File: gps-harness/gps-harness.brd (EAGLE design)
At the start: 29.6 x 33.9 mm, 7 parts

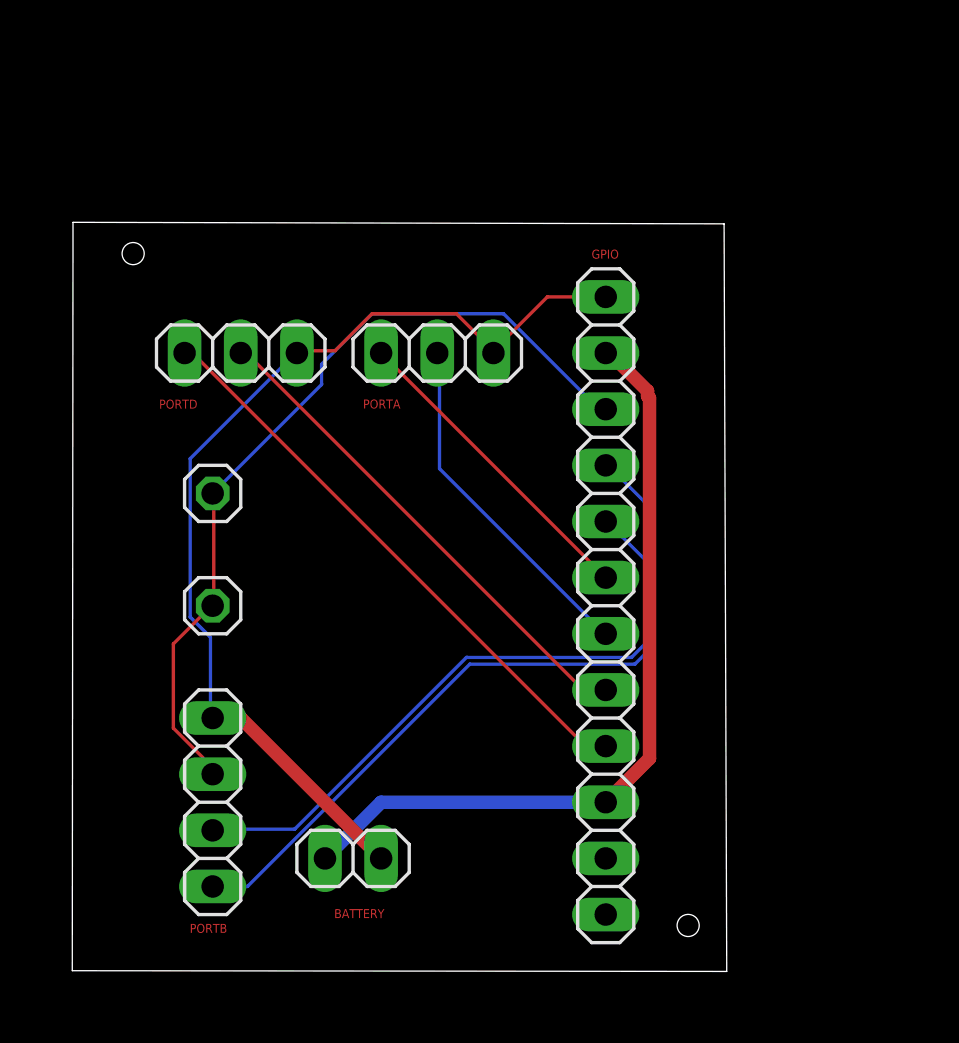
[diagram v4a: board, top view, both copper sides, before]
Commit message: Change Schematic to Parts by parts
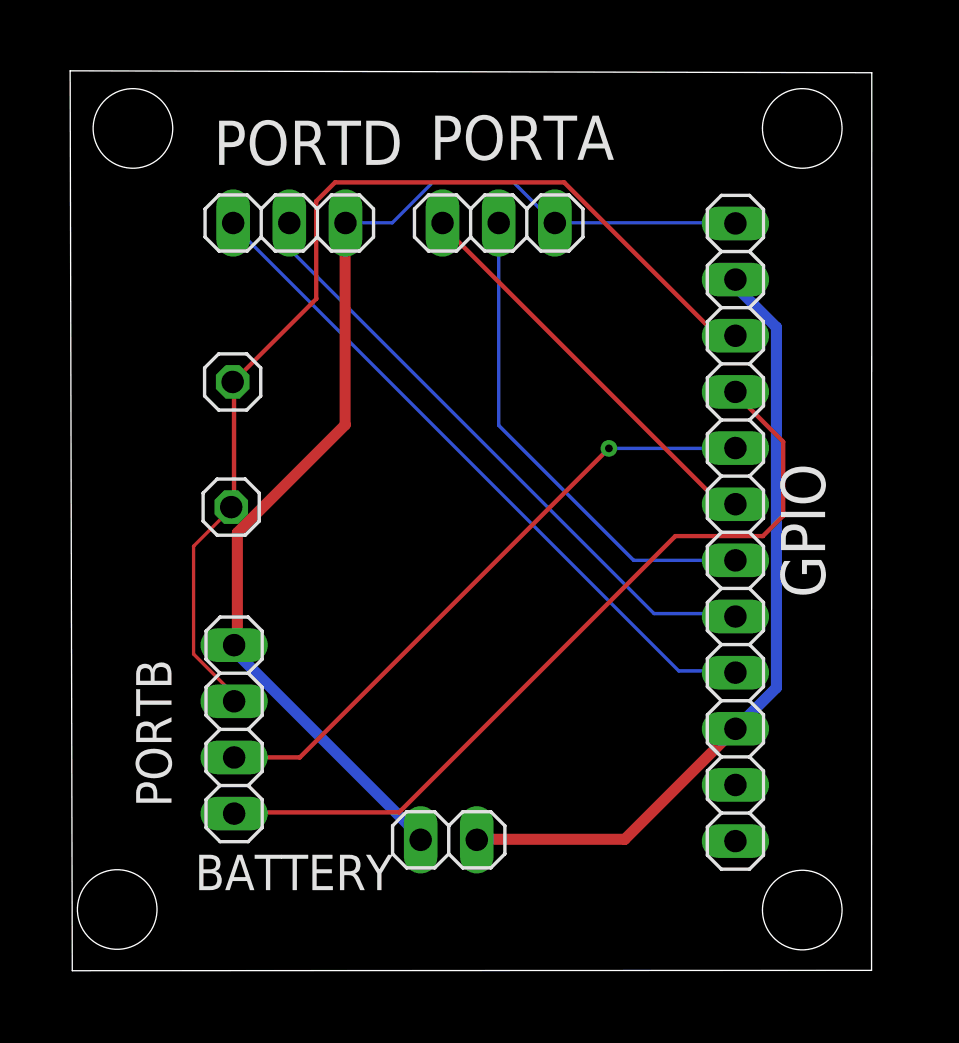
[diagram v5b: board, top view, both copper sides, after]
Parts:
- moved GPIO 6.74 mm to (30.0, 19.8)
- moved PORTA 6.51 mm to (19.3, 33.8)
- moved PORTD 6.28 mm to (9.82, 33.8)
- moved IMU 5.12 mm to (7.25, 26.6)
- moved TSY 4.54 mm to (7.19, 21.0)
- moved BATTERY 4.41 mm to (17.0, 5.92), turned to 180 degrees
- moved PORTB 3.44 mm to (7.32, 10.9)
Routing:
- net IMU: track 37.7 -> 47.9 mm
- net GND: track 45.8 -> 54.2 mm
- net RXA: track 15.9 -> 22.5 mm
- net RXD: track 22.9 -> 28.2 mm
- net TXD: track 26.4 -> 31.2 mm
- net TXA: track 14.4 -> 18.6 mm
- net TXB: track 33.5 -> 36.9 mm
- net RXB: track 29.3 -> 28.7 mm, vias 0 -> 1
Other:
- board size 29.6 x 33.9 mm -> 36.3 x 40.7 mm
- board text added: "Autorally GPS Harness v1.0 Oct. 2019"
- board text added: "IMU"
- board text added: "TSM"

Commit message: Reroute the board
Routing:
- net IMU: track 47.9 -> 39.9 mm, vias 0 -> 2
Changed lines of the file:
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@@
 <wire x1="7.3152" y1="12.192" x2="7.320278125" y2="12.186921875" width="0.1524" layer="1"/>
 <wire x1="7.1628" y1="20.8788" x2="7.1882" y2="20.9702375" width="0.1524" layer="1"/>
-<wire x1="29.1084" y1="28.8036" x2="29.8704" y2="28.8036" width="0.1524" layer="1"/>
-<wire x1="22.2504" y1="35.6616" x2="29.1084" y2="28.8036" width="0.2" layer="1"/>
-<wire x1="11.8872" y1="35.6616" x2="22.2504" y2="35.6616" width="0.2" layer="1"/>
-<wire x1="11.0363" y1="34.8107" x2="11.8872" y2="35.6616" width="0.2" layer="1"/>
-<wire x1="11.0363" y1="30.3911" x2="11.0363" y2="34.8107" width="0.2" layer="1"/>
-<wire x1="7.3152" y1="26.67" x2="11.0363" y2="30.3911" width="0.2" layer="1"/>
 <wire x1="29.8704" y1="28.8036" x2="29.9974" y2="28.722315625" width="0.1524" layer="1"/>
 <wire x1="7.3152" y1="26.67" x2="7.254240625" y2="26.6319" width="0.1524" layer="1"/>
+<wire x1="7.254240625" y1="26.6319" x2="13.30451875" y2="26.6319" width="0.1524" layer="16"/>
+<wire x1="13.30451875" y1="26.6319" x2="13.307059375" y2="26.634440625" width="0.1524" layer="16"/>
+<via x="13.307059375" y="26.634440625" extent="1-16" drill="0.35"/>
+<wire x1="13.307059375" y1="26.634440625" x2="17.983203125" y2="26.634440625" width="0.1524" layer="1"/>
+<wire x1="17.983203125" y1="26.634440625" x2="20.10918125" y2="28.76041875" width="0.1524" layer="1"/>
+<wire x1="20.10918125" y1="28.76041875" x2="20.114259375" y2="28.76041875" width="0.1524" layer="1"/>
+<via x="20.114259375" y="28.76041875" extent="1-16" drill="0.35"/>
+<wire x1="20.114259375" y1="28.76041875" x2="26.418540625" y2="28.76041875" width="0.1524" layer="16"/>
+<wire x1="26.418540625" y1="28.76041875" x2="26.42108125" y2="28.762959375" width="0.1524" layer="16"/>
+<wire x1="26.42108125" y1="28.762959375" x2="29.95675625" y2="28.762959375" width="0.1524" layer="16"/>
+<wire x1="29.95675625" y1="28.762959375" x2="29.9974" y2="28.722315625" width="0.1524" layer="16"/>
 </signal>
 <signal name="N$23">

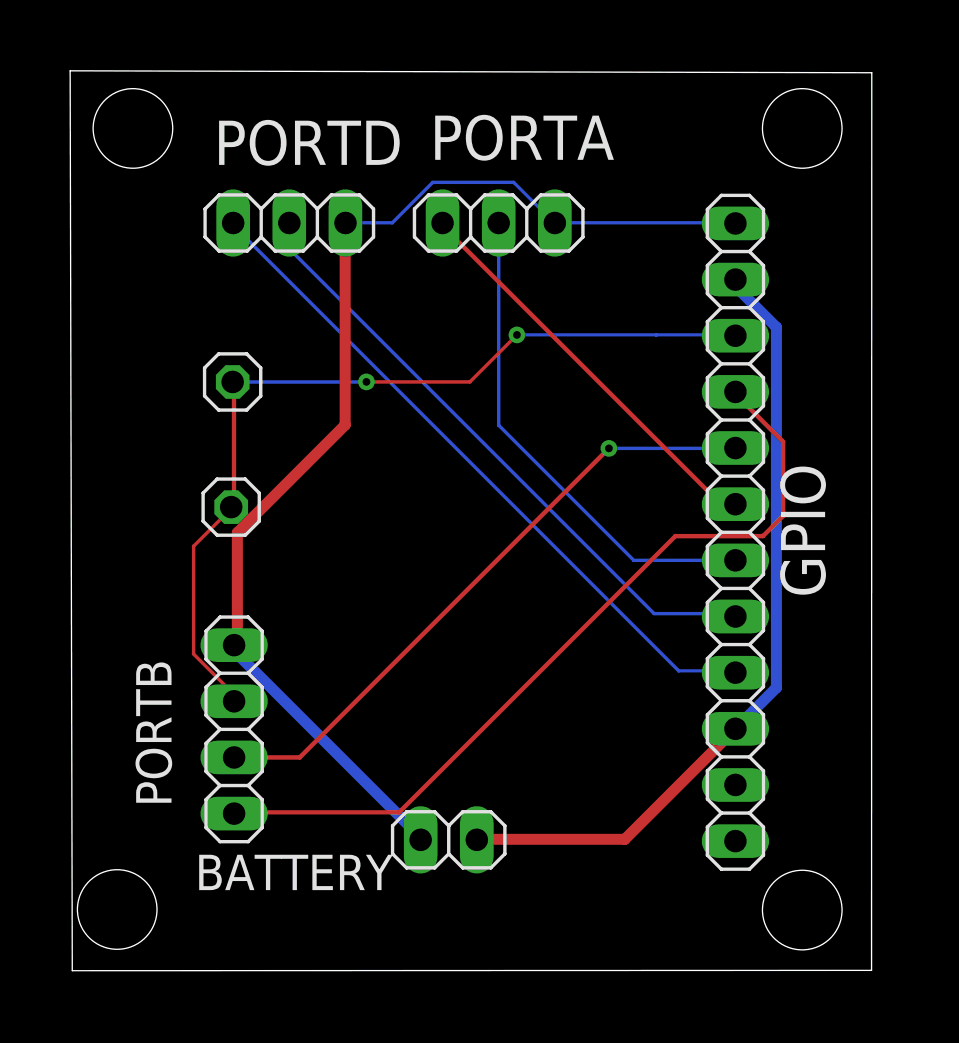
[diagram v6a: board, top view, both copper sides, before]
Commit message: Add GND Plane
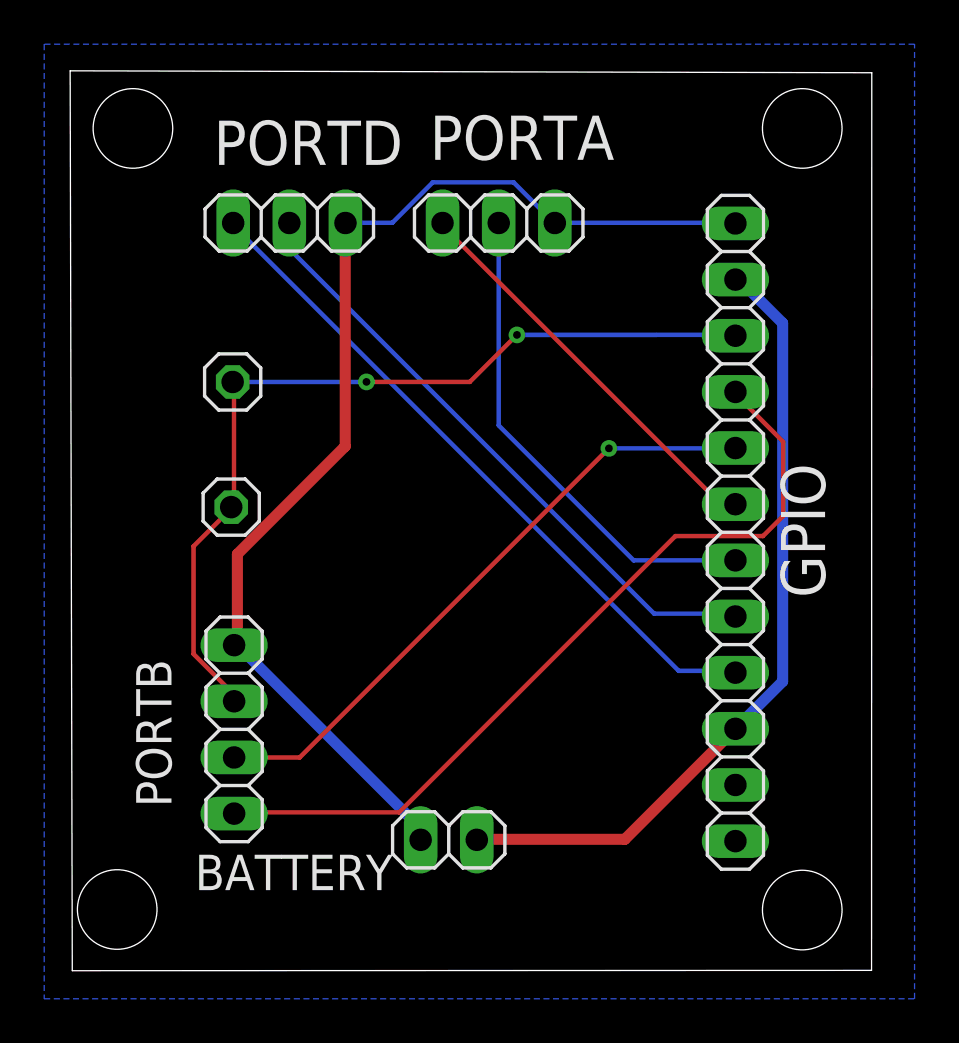
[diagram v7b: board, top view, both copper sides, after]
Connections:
- removed net N$23: GPIO.11
- removed net N$24: GPIO.12
- new net NO_CONNECTION: GPIO.11, GPIO.12
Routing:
- net GND: track 54.2 -> 53.3 mm
- added copper zone on layer 16, net GND

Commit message: Add GND PLane & clearify the fastner of the right bottom driller, regorup rhe schematic
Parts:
- moved GPIO 1.27 mm to (28.7, 19.8)
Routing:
- net TXB: track 36.9 -> 35.6 mm
- net TXD: track 31.2 -> 29.9 mm
- net RXD: track 28.2 -> 27.0 mm
- net RXB: track 28.5 -> 27.2 mm
- net RXA: track 22.4 -> 21.1 mm
- net GND: track 53.3 -> 52.0 mm
- net IMU: track 39.6 -> 38.4 mm
- net TXA: track 18.6 -> 18.0 mm
